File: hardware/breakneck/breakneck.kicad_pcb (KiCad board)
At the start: 2 copper layers, 53.3 x 64 mm, 109 parts, among them J1 CONN_WEST, J10 GS2, J12 CONN_JTAG_6P, J15 GS2, J16 CONN_JST, J2 CONN_DEDI, J3 CONN_OLED, J4 USB_C_Receptacle, J5 CONN_SOUTH, J6 CONN_EAST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

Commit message: Flushed current changes to accommodate results of recent assembly tests; Introduced plastics engineering resources, made fiducial marks SMT for placing, merged SMT attribute to panel design accordingly, removed incomplete test point symbol, and sanitised private file path.
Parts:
- FID2, FID4, FID6: footprint Monero_Local:Fiducial_1mm_Dia_2.54mm_Outer_CopperBottom -> Monero_Local:Fiducial_1mm_Dia_2.54mm_Outer_CopperTop; moved to B.Cu
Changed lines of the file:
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@@
     (add_net "Net-(U4-Pad28)")
   )
+  (module Monero_Local:Fiducial_1mm_Dia_2.54mm_Outer_CopperTop (layer B.Cu)
+    (at 151 126)
+    (descr "Circular Fiducial, 1mm bare copper top; 2.54mm keepout")
+    (tags marker)
+    (attr smd)
+    (fp_text reference FID6 (at 3.4 -0.7) (layer B.SilkS) hide
+      (effects (font (size 1 1) (thickness 0.15)) (justify mirror))
+    )
+    (fp_text value Fiducial-PCB (at 0 1.8) (layer B.Fab)
+      (effects (font (size 1 1) (thickness 0.15)) (justify mirror))
+    )
+    (fp_circle (center 0 0) (end 1.55 0) (layer B.CrtYd) (width 0.05))
+    (pad ~ smd circle (at 0 0) (size 1 1) (layers B.Cu B.Mask)
+      (net 55 "Net-(FID6-Pad~)") (solder_mask_margin 0.77) (clearance 0.77))
+  )
+  (module Monero_Local:Fiducial_1mm_Dia_2.54mm_Outer_CopperTop (layer B.Cu)
+    (at 151 66)
+    (descr "Circular Fiducial, 1mm bare copper top; 2.54mm keepout")
+    (tags marker)
+    (attr smd)
+    (fp_text reference FID4 (at 3.4 -0.7) (layer B.SilkS) hide
+      (effects (font (size 1 1) (thickness 0.15)) (justify mirror))
+    )
+    (fp_text value Fiducial-PCB (at 0 1.8) (layer B.Fab)
+      (effects (font (size 1 1) (thickness 0.15)) (justify mirror))
+    )
+    (fp_circle (center 0 0) (end 1.55 0) (layer B.CrtYd) (width 0.05))
+    (pad ~ smd circle (at 0 0) (size 1 1) (layers B.Cu B.Mask)
+      (net 23 "Net-(FID4-Pad~)") (solder_mask_margin 0.77) (clearance 0.77))
+  )
+  (module Monero_Local:Fiducial_1mm_Dia_2.54mm_Outer_CopperTop (layer B.Cu)
+    (at 102 66)
+    (descr "Circular Fiducial, 1mm bare copper top; 2.54mm keepout")
+    (tags marker)
+    (attr smd)
+    (fp_text reference FID2 (at 3.4 -0.7) (layer B.SilkS) hide
+      (effects (font (size 1 1) (thickness 0.15)) (justify mirror))
+    )
+    (fp_text value Fiducial-PCB (at 0 1.8) (layer B.Fab)
+      (effects (font (size 1 1) (thickness 0.15)) (justify mirror))
+    )
+    (fp_circle (center 0 0) (end 1.55 0) (layer B.CrtYd) (width 0.05))
+    (pad ~ smd circle (at 0 0) (size 1 1) (layers B.Cu B.Mask)
+      (net 21 "Net-(FID2-Pad~)") (solder_mask_margin 0.77) (clearance 0.77))
+  )
   (module Monero_Local:TestPoint_THTPad_D1.5mm_Drill0.7mm (layer F.Cu)
     (at 130.8 95)
@@
     (descr "Circular Fiducial, 1mm bare copper top; 2.54mm keepout")
     (tags marker)
-    (attr virtual)
+    (attr smd)
     (fp_text reference FID1 (at 3.4 0.7) (layer F.SilkS) hide
       (effects (font (size 1 1) (thickness 0.15)))
@@
       (net 20 "Net-(FID1-Pad~)") (solder_mask_margin 0.77) (clearance 0.77))
   )
-  (module Monero_Local:Fiducial_1mm_Dia_2.54mm_Outer_CopperBottom (layer F.Cu)
-    (at 102 66)
-    (descr "Circular Fiducial, 1mm bare copper bottom; 2.54mm keepout")
-    (tags marker)
-    (attr virtual)
-    (fp_text reference FID2 (at 3.4 0.7) (layer F.SilkS) hide
-      (effects (font (size 1 1) (thickness 0.15)))
-    )
-    (fp_text value Fiducial-PCB (at 0 -1.8) (layer F.Fab)
-      (effects (font (size 1 1) (thickness 0.15)))
-    )
-    (fp_circle (center 0 0) (end 1.55 0) (layer B.CrtYd) (width 0.05))
-    (pad ~ smd circle (at 0 0) (size 1 1) (layers B.Cu B.Mask)
-      (net 21 "Net-(FID2-Pad~)") (solder_mask_margin 0.77) (clearance 0.77))
-  )
   (module Monero_Local:Fiducial_1mm_Dia_2.54mm_Outer_CopperTop (layer F.Cu)
     (at 151 66)
     (descr "Circular Fiducial, 1mm bare copper top; 2.54mm keepout")
     (tags marker)
-    (attr virtual)
+    (attr smd)
     (fp_text reference FID3 (at 3.4 0.7) (layer F.SilkS) hide
       (effects (font (size 1 1) (thickness 0.15)))
@@
       (net 22 "Net-(FID3-Pad~)") (solder_mask_margin 0.77) (clearance 0.77))
   )
-  (module Monero_Local:Fiducial_1mm_Dia_2.54mm_Outer_CopperBottom (layer F.Cu)
-    (at 151 66)
-    (descr "Circular Fiducial, 1mm bare copper bottom; 2.54mm keepout")
-    (tags marker)
-    (attr virtual)
-    (fp_text reference FID4 (at 3.4 0.7) (layer F.SilkS) hide
-      (effects (font (size 1 1) (thickness 0.15)))
-    )
-    (fp_text value Fiducial-PCB (at 0 -1.8) (layer F.Fab)
-      (effects (font (size 1 1) (thickness 0.15)))
-    )
-    (fp_circle (center 0 0) (end 1.55 0) (layer B.CrtYd) (width 0.05))
-    (pad ~ smd circle (at 0 0) (size 1 1) (layers B.Cu B.Mask)
-      (net 23 "Net-(FID4-Pad~)") (solder_mask_margin 0.77) (clearance 0.77))
-  )
-  (module Monero_Local:Fiducial_1mm_Dia_2.54mm_Outer_CopperBottom (layer F.Cu)
-    (at 151 126)
-    (descr "Circular Fiducial, 1mm bare copper bottom; 2.54mm keepout")
-    (tags marker)
-    (attr virtual)
-    (fp_text reference FID6 (at 3.4 0.7) (layer F.SilkS) hide
-      (effects (font (size 1 1) (thickness 0.15)))
-    )
-    (fp_text value Fiducial-PCB (at 0 -1.8) (layer F.Fab)
-      (effects (font (size 1 1) (thickness 0.15)))
-    )
-    (fp_circle (center 0 0) (end 1.55 0) (layer B.CrtYd) (width 0.05))
-    (pad ~ smd circle (at 0 0) (size 1 1) (layers B.Cu B.Mask)
-      (net 55 "Net-(FID6-Pad~)") (solder_mask_margin 0.77) (clearance 0.77))
-  )
   (module Monero_Local:Pin_Header_Straight_1x20_Pitch2.54mm (layer F.Cu)
     (at 102.54 72.12)
@@
     (descr "Circular Fiducial, 1mm bare copper top; 2.54mm keepout")
     (tags marker)
-    (attr virtual)
+    (attr smd)
     (fp_text reference FID5 (at 3.4 0.7) (layer F.SilkS) hide
       (effects (font (size 1 1) (thickness 0.15)))

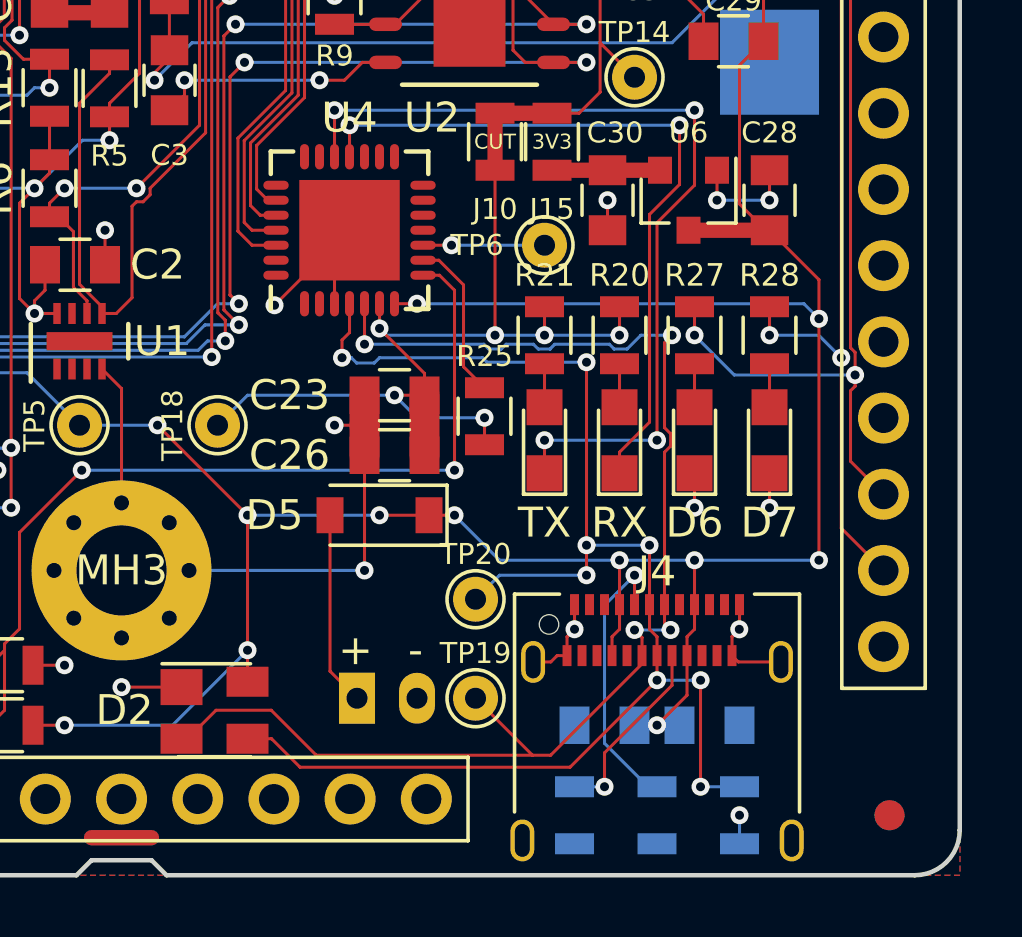
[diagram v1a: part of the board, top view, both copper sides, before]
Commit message: Completed USBC debugging structures, including removal of unused contacts, symbol adaptation, introduction of solderbridges, test point connections, and complete segregation of inner row USBC connector pads.
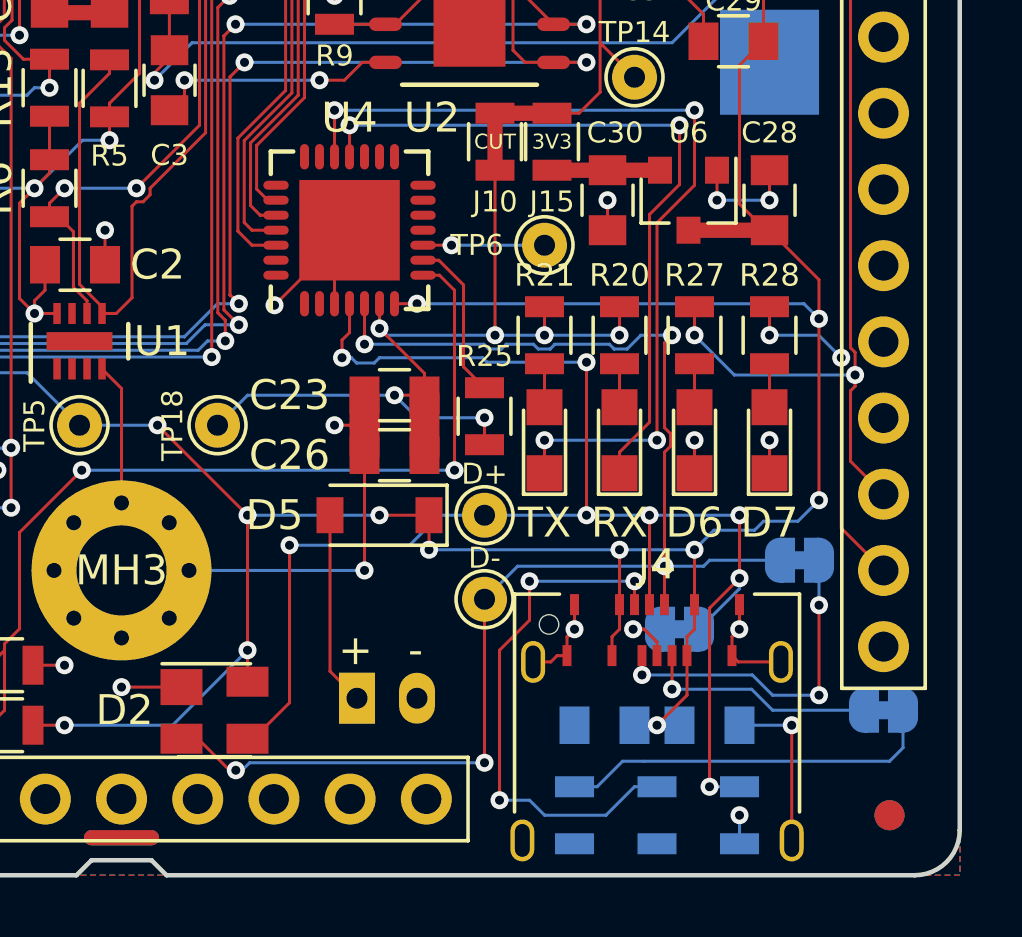
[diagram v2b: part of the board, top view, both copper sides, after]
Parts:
- added JCC: SJC2, Monero_Local:Solderjump-2NCRndpad, B.Cu at (150.8, 122.5)
- added JDM: SJC2, Monero_Local:Solderjump-2NCRndpad, B.Cu at (148.0, 117.5)
- added JDP: SJC2, Monero_Local:Solderjump-2NCRndpad, B.Cu at (144.0, 119.8)
- J4: value USB_C_Receptacle -> USB_C_Rcpt_Min; footprint Monero_Local:USB_C_Receptacle_Amphenol_12401610E4-2A -> Monero_Local:USBC_Rcpt_Min_12401610E4-2A
- moved D- 3.31 mm to (137.5, 118.8)
- moved D+ 2.82 mm to (137.5, 116.0)
- renumbered TP20 to D+, TP19 to D-
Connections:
- J4 pad B6: /USB_P -> Net-(J4-PadB6)
- J4 pad B7: /USB_N -> Net-(J4-PadB7)
- MH1 pad : GND -> (no net)
- MH2 pad : GND -> (no net)
- MH3 pad : GND -> (no net)
- R16 pad 2: Net-(J4-PadB5) -> Net-(JP5-Pad2)
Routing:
- net Net-(JP5-Pad2): track 0.00 -> 12.7 mm
- net Net-(J4-PadB7): track 0.00 -> 11.3 mm, vias 0 -> 3
- net Net-(J4-PadA5): track 9.34 -> 17.8 mm, vias 1 -> 3
- net GND: track 213.0 -> 218.5 mm, vias 42 -> 43
- net /USB_P: track 49.7 -> 53.6 mm
- net /USB_N: track 45.1 -> 47.9 mm, vias 4 -> 5
- net Net-(J4-PadB6): track 0.00 -> 2.32 mm, vias 0 -> 1
- net Net-(J4-PadB5): track 6.30 -> 7.81 mm
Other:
- board text added: "Fifth generation prototype RFC-HWALLET-1 ET1 Extra Tabulo, by the Monero Hardware Team CERN OSH License, © 2018 The Monero Project"
- board text removed: "Fifth generation prototype RFC-HWALLET-1 ET0 Extra Tabulo, by the Monero Hardware Team CERN OSH License, © 2018 The Monero Project"
